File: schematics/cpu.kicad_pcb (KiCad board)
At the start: 2 copper layers, 33 parts, among them J1 Conn_01x01, J2 Conn_01x01, J3 Conn_01x01, J4 Conn_01x01, J5 Conn_01x01, J6 Conn_01x01, U1 74LS86, U10 74HC245, U11 74HC245, U2 74LS86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

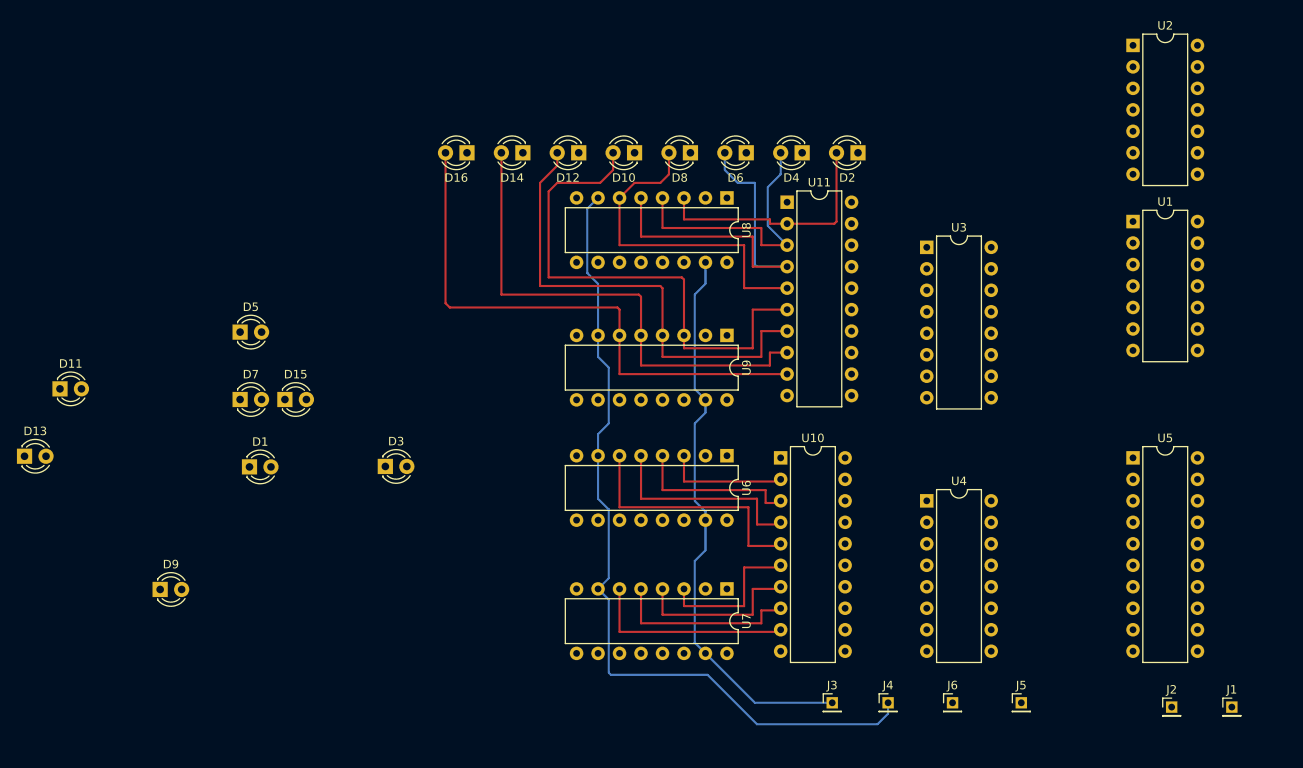
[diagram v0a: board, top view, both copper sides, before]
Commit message: Finished placing tracks for the registers and ALU PCB.
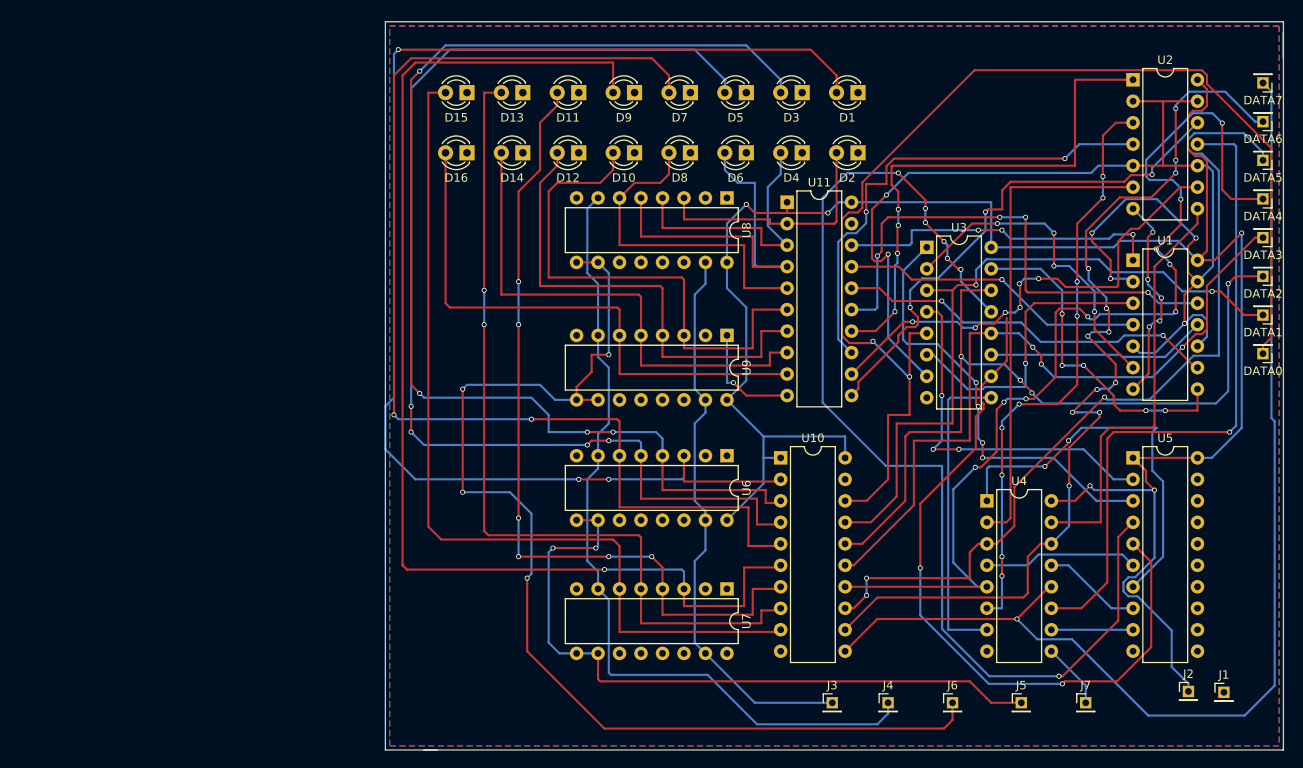
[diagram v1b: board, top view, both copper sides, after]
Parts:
- added DATA0: Conn_01x01, Pin_Headers:Pin_Header_Straight_1x01_Pitch2.00mm, F.Cu at (183.5, 113.7)
- added DATA1: Conn_01x01, Pin_Headers:Pin_Header_Straight_1x01_Pitch2.00mm, F.Cu at (183.5, 109.1)
- added DATA2: , Pin_Headers:Pin_Header_Straight_1x01_Pitch2.00mm, F.Cu at (183.5, 104.5)
- added DATA3: Conn_01x01, Pin_Headers:Pin_Header_Straight_1x01_Pitch2.00mm, F.Cu at (183.5, 99.9)
- added DATA4: Conn_01x01, Pin_Headers:Pin_Header_Straight_1x01_Pitch2.00mm, F.Cu at (183.5, 95.4)
- added DATA5: Conn_01x01, Pin_Headers:Pin_Header_Straight_1x01_Pitch2.00mm, F.Cu at (183.5, 90.8)
- added DATA6: Conn_01x01, Pin_Headers:Pin_Header_Straight_1x01_Pitch2.00mm, F.Cu at (183.5, 86.2)
- added DATA7: Conn_01x01, Pin_Headers:Pin_Header_Straight_1x01_Pitch2.00mm, F.Cu at (183.5, 81.7)
- added J7: Conn_01x01, Pin_Headers:Pin_Header_Straight_1x01_Pitch2.00mm, F.Cu at (162.6, 154.9)
- moved D1 84.5 mm to (135.6, 82.8), turned to 180 degrees
- moved D9 81.2 mm to (109.2, 82.8), turned to 180 degrees
- moved D13 72.9 mm to (96.0, 82.8), turned to 180 degrees
- moved D11 70.6 mm to (102.6, 82.8), turned to 180 degrees
- moved D5 66.2 mm to (122.4, 82.8), turned to 180 degrees
- moved D3 66.2 mm to (129.0, 82.8), turned to 180 degrees
- moved D7 64.4 mm to (115.8, 82.8), turned to 180 degrees
- moved D15 42.2 mm to (89.4, 82.8), turned to 180 degrees
- moved U4 7.11 mm to (150.9, 131.1)
- moved U1 4.57 mm to (168.1, 102.6)
- moved U2 4.06 mm to (168.1, 81.3)
- moved J2 2.71 mm to (174.7, 153.6)
- moved J1 1.98 mm to (178.9, 153.7)
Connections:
- J2 pad 1: +5V -> VCC
- U10 pad 1: +5V -> VCC
- U11 pad 1: +5V -> VCC
- U5 pad 1: +5V -> VCC
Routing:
- net VCC: track 0.00 -> 236.9 mm, vias 0 -> 5
- net Net-(U1-Pad10): track 0.00 -> 147.5 mm, vias 0 -> 6
- net Net-(D1-Pad2): track 14.7 -> 157.1 mm, vias 0 -> 3
- net Net-(DATA0-Pad1): track 0.00 -> 140.9 mm, vias 0 -> 2
- net Net-(DATA7-Pad1): track 0.00 -> 136.0 mm, vias 0 -> 1
- net Net-(J6-Pad1): track 0.00 -> 133.4 mm, vias 0 -> 5
- net Net-(U3-Pad13): track 0.00 -> 130.2 mm, vias 0 -> 7
- net Net-(D9-Pad2): track 18.3 -> 140.9 mm, vias 0 -> 1
- net Net-(DATA4-Pad1): track 0.00 -> 122.3 mm, vias 0 -> 9
- net Net-(D3-Pad2): track 19.8 -> 140.0 mm, vias 0 -> 4
- net Net-(DATA6-Pad1): track 0.00 -> 115.3 mm, vias 0 -> 12
- net Net-(D5-Pad2): track 24.9 -> 137.2 mm, vias 0 -> 4
- net Net-(D7-Pad2): track 30.0 -> 137.4 mm, vias 0 -> 2
- net Net-(DATA5-Pad1): track 0.00 -> 101.2 mm, vias 0 -> 3
- net Net-(DATA2-Pad1): track 0.00 -> 95.7 mm, vias 0 -> 4
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- added copper zone on B.Cu, net GND
- added copper zone on F.Cu, net GND
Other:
- board outline added: 106.2 x 86.1 mm
